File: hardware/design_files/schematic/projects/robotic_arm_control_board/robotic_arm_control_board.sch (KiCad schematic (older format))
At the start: 13 parts, among them J1 SERVO_INTERFACE, J2 GPIO, J3 9-12V, U1 LM2576HVS-ADJ

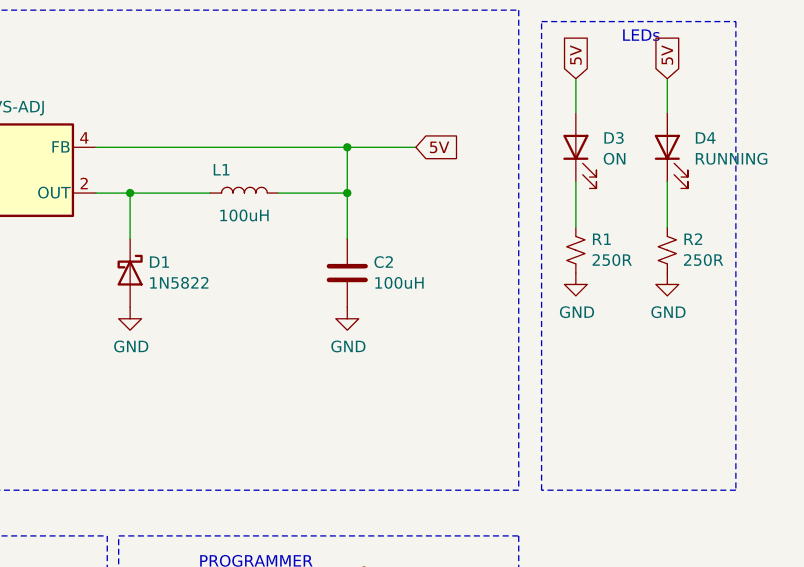
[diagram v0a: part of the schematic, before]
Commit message: finish creating PCB
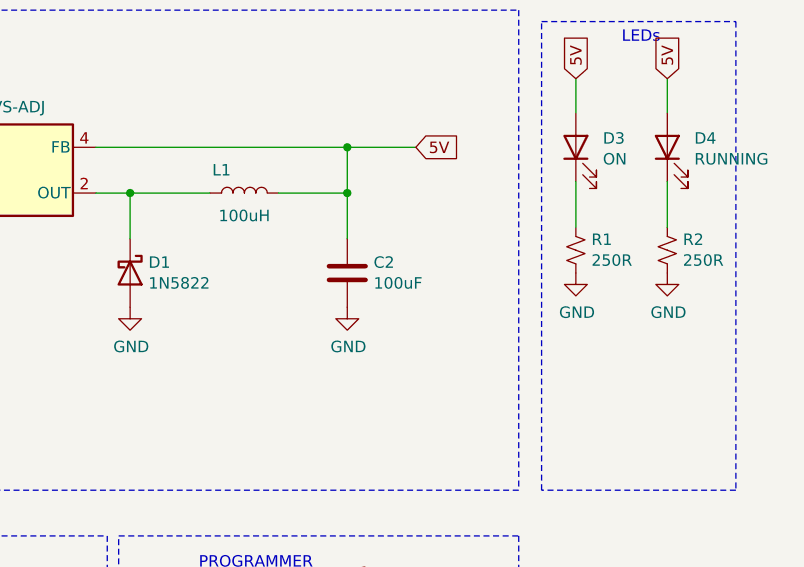
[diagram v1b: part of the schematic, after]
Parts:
- C2: value 100uH -> 100uF; footprint Inductor_SMD:L_1008_2520Metric -> Capacitor_SMD:CP_Elec_8x6.7
- L1: footprint (none) -> Inductor_THT:L_Axial_L13.0mm_D4.5mm_P7.62mm_Vertical_Fastron_HCCC
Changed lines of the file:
@@
-$EndComp
-$Comp
-L Device:C C2
-U 1 1 60FAE532
-P 7500 1850
-F 0 "C2" H 7615 1896 50  0000 L CNN
-F 1 "100uH" H 7615 1805 50  0000 L CNN
-F 2 "Inductor_SMD:L_1008_2520Metric" H 7538 1700 50  0001 C CNN
-F 3 "~" H 7500 1850 50  0001 C CNN
-	1    7500 1850
-	1    0    0    -1
 $EndComp
 $Comp
@@
 F 0 "L1" V 7150 1600 50  0000 C CNN
 F 1 "100uH" V 6950 1500 50  0000 C CNN
-F 2 "" H 7050 1500 50  0001 C CNN
+F 2 "Inductor_THT:L_Axial_L13.0mm_D4.5mm_P7.62mm_Vertical_Fastron_HCCC" H 7050 1500 50  0001 C CNN
 F 3 "~" H 7050 1500 50  0001 C CNN
 	1    7050 1500
@@
 	1    0    0    -1
 $EndComp
+$Comp
+L Device:C C2
+U 1 1 61063888
+P 7500 1850
+F 0 "C2" H 7615 1896 50  0000 L CNN
+F 1 "100uF" H 7615 1805 50  0000 L CNN
+F 2 "Capacitor_SMD:CP_Elec_8x6.7" H 7538 1700 50  0001 C CNN
+F 3 "~" H 7500 1850 50  0001 C CNN
+	1    7500 1850
+	1    0    0    -1
+$EndComp
